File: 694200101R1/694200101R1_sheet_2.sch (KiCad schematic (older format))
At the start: 87 parts, among them U4 M24M02-DRMN6TP, U5 IS31FL3733B-QFLS4-TR, U6 IS31FL3733B-QFLS4-TR

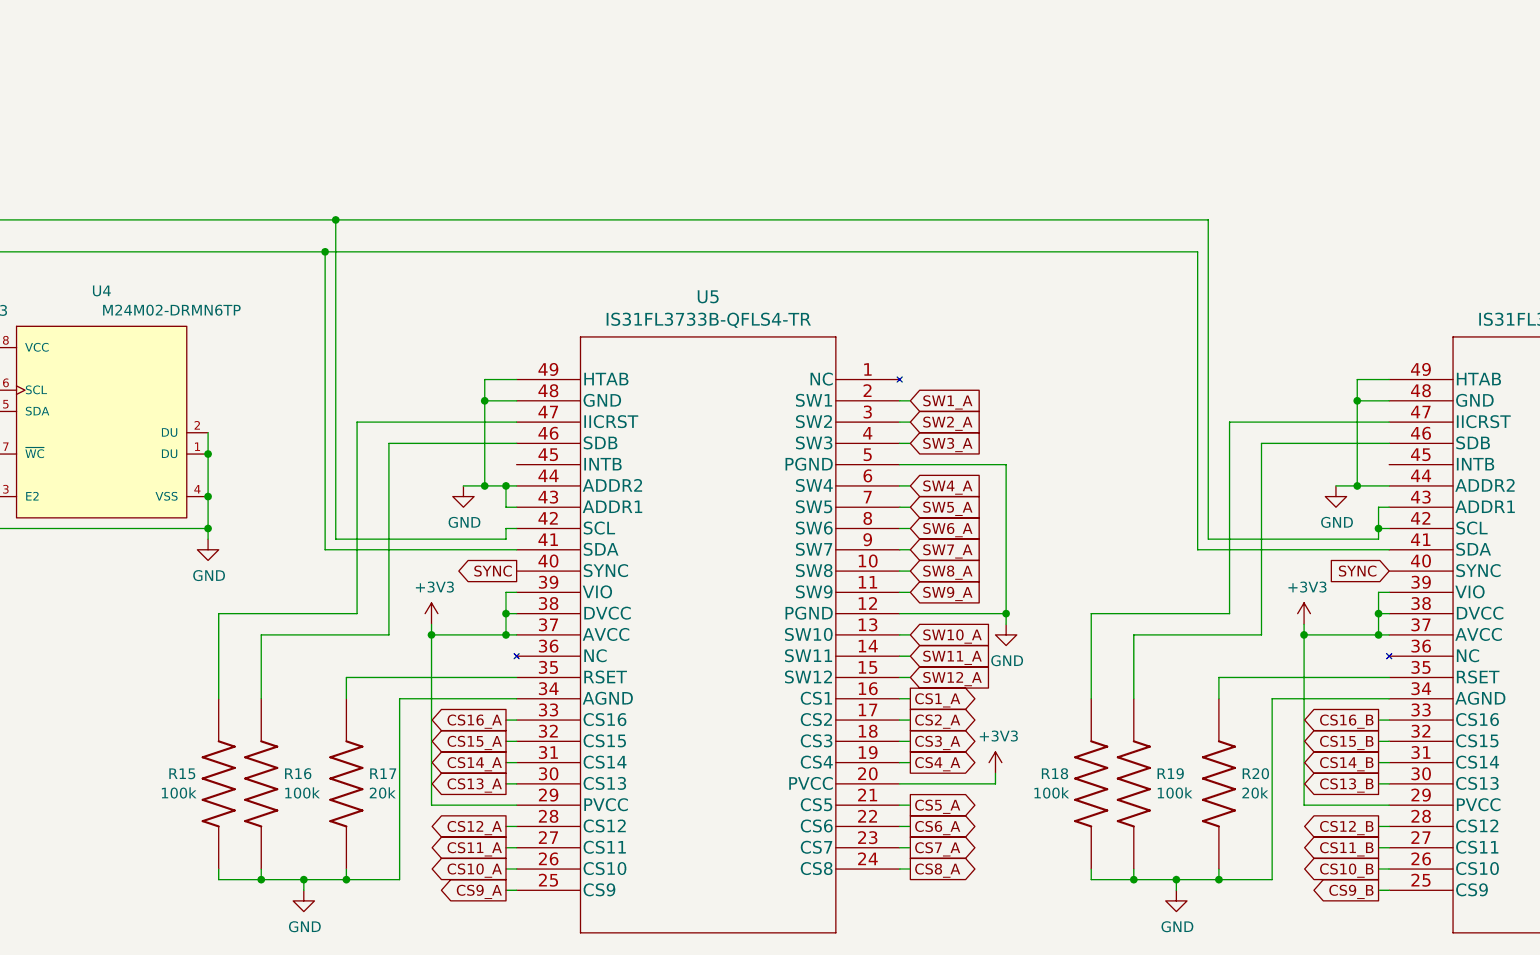
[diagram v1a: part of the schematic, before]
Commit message: Fixed incorrect pull-down resistors
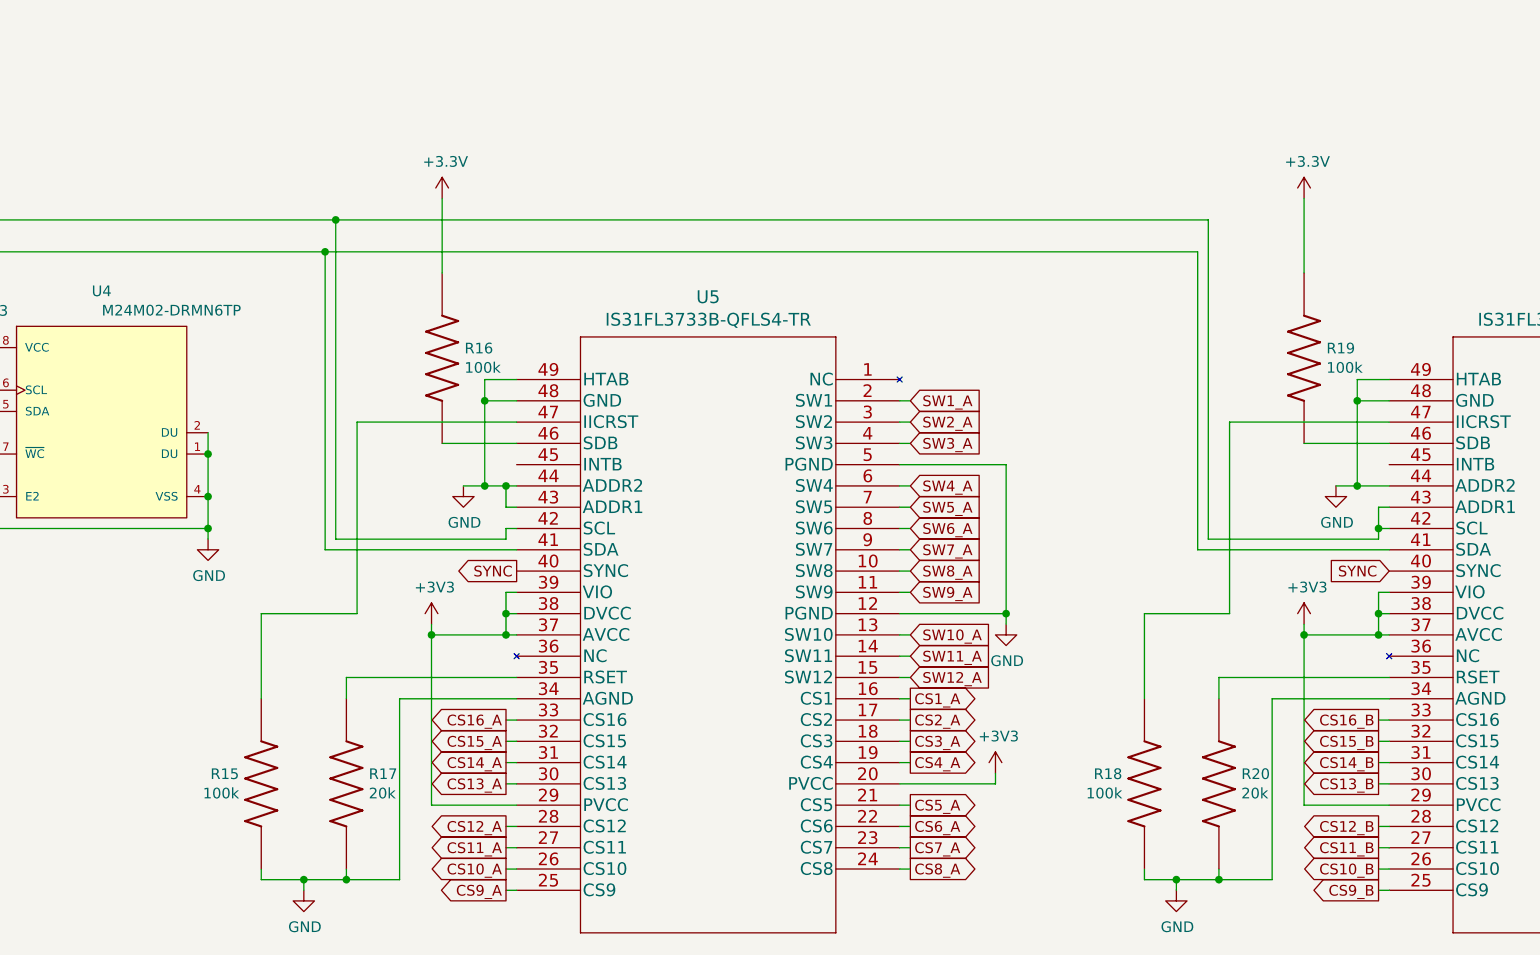
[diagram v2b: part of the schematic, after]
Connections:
- net +3V3: now also R16.1, R19.1
- net GND: no longer R16.2, R19.2
- net at U5.46 (SDB): now also R16.2; no longer R16.1
- net at U6.46 (SDB): now also R19.2; no longer R19.1
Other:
- moved on the sheet: R15, R16, R18, R19
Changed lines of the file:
@@
 LED_DRIVER_A\nPWR_FILTER
 Wire Wire Line
-	4000 8050 3400 8050
-Wire Wire Line
-	3400 8050 3400 8950
-Wire Wire Line
-	3400 8950 2800 8950
-Wire Wire Line
-	2800 8950 2800 9250
+	4000 8050 3650 8050
 Connection ~ 3600 8950
 Wire Wire Line
@@
 	3250 7950 3250 8850
 Wire Wire Line
-	3250 8850 2600 8850
+	3250 8850 2800 8850
 Wire Wire Line
-	2600 8850 2600 9250
+	2800 8850 2800 9250
 Wire Wire Line
-	2600 10050 2600 10100
-Wire Wire Line
-	2800 10100 2800 10050
+	2800 10050 2800 10100
 Wire Wire Line
 	4000 9250 3450 9250
@@
 Wire Wire Line
 	3450 10100 3200 10100
-Connection ~ 2800 10100
-Wire Wire Line
-	2600 10100 2800 10100
 Wire Wire Line
 	3600 8900 3600 8950
@@
 Connection ~ 3000 10100
 Wire Wire Line
-	3000 10100 2800 10100
-Wire Wire Line
 	3950 8950 3600 8950
 Wire Wire Line
@@
 Connection ~ 8050 8850
 Connection ~ 8050 8950
-Wire Wire Line
-	8100 8050 7500 8050
-Wire Wire Line
-	7500 8050 7500 8950
-Wire Wire Line
-	7500 8950 6900 8950
-Wire Wire Line
-	6900 8950 6900 9250
 Connection ~ 7700 8950
 Wire Wire Line
@@
 	7350 7950 7350 8850
 Wire Wire Line
-	7350 8850 6700 8850
-Wire Wire Line
-	6700 8850 6700 9250
+	7350 8850 6950 8850
 Wire Wire Line
-	6700 10050 6700 10100
+	6950 8850 6950 9250
 Wire Wire Line
-	6900 10100 6900 10050
+	6950 10050 6950 10100
 Wire Wire Line
 	8100 9250 7550 9250
@@
 Wire Wire Line
 	7550 10100 7300 10100
-Connection ~ 6900 10100
-Wire Wire Line
-	6700 10100 6900 10100
 Wire Wire Line
 	7700 8900 7700 8950
@@
 Connection ~ 7100 10100
 Wire Wire Line
-	7100 10100 6900 10100
-Wire Wire Line
 	8050 8950 7700 8950
 Wire Wire Line
@@
 L Resistor-Lib:RMCF0603FT100K R16
 U 1 1 63EAB8BE
-P 2800 9650
-F 0 "R16" V 2754 9755 50  0000 L CNN
-F 1 "RMCF0603FT100K" H 2500 9450 50  0001 L BNN
-F 2 "Resistor-Libs:RESC1508X55N" H 2800 9650 50  0001 L BNN
-F 3 "" H 2800 9650 50  0001 L BNN
-F 4 "100k" V 2845 9755 50  0000 L CNN "resistance"
-	1    2800 9650
+P 3650 7650
+F 0 "R16" V 3604 7755 50  0000 L CNN
+F 1 "RMCF0603FT100K" H 3350 7450 50  0001 L BNN
+F 2 "Resistor-Libs:RESC1508X55N" H 3650 7650 50  0001 L BNN
+F 3 "" H 3650 7650 50  0001 L BNN
+F 4 "100k" V 3695 7755 50  0000 L CNN "resistance"
+	1    3650 7650
 	0    1    1    0
 $EndComp
@@
 L Resistor-Lib:RMCF0603FT100K R15
 U 1 1 63EB01BF
-P 2600 9650
-F 0 "R15" V 2554 9546 50  0000 R CNN
-F 1 "RMCF0603FT100K" H 2300 9450 50  0001 L BNN
-F 2 "Resistor-Libs:RESC1508X55N" H 2600 9650 50  0001 L BNN
-F 3 "" H 2600 9650 50  0001 L BNN
-F 4 "100k" V 2645 9546 50  0000 R CNN "resistance"
-	1    2600 9650
+P 2800 9650
+F 0 "R15" V 2754 9546 50  0000 R CNN
+F 1 "RMCF0603FT100K" H 2500 9450 50  0001 L BNN
+F 2 "Resistor-Libs:RESC1508X55N" H 2800 9650 50  0001 L BNN
+F 3 "" H 2800 9650 50  0001 L BNN
+F 4 "100k" V 2845 9546 50  0000 R CNN "resistance"
+	1    2800 9650
 	0    1    1    0
 $EndComp
@@
 L Resistor-Lib:RMCF0603FT100K R19
 U 1 1 6409AB23
-P 6900 9650
-F 0 "R19" V 6854 9755 50  0000 L CNN
-F 1 "RMCF0603FT100K" H 6600 9450 50  0001 L BNN
-F 2 "Resistor-Libs:RESC1508X55N" H 6900 9650 50  0001 L BNN
-F 3 "" H 6900 9650 50  0001 L BNN
-F 4 "100k" V 6945 9755 50  0000 L CNN "resistance"
-	1    6900 9650
+P 7700 7650
+F 0 "R19" V 7654 7755 50  0000 L CNN
+F 1 "RMCF0603FT100K" H 7400 7450 50  0001 L BNN
+F 2 "Resistor-Libs:RESC1508X55N" H 7700 7650 50  0001 L BNN
+F 3 "" H 7700 7650 50  0001 L BNN
+F 4 "100k" V 7745 7755 50  0000 L CNN "resistance"
+	1    7700 7650
 	0    1    1    0
 $EndComp
@@
 L Resistor-Lib:RMCF0603FT100K R18
 U 1 1 6409AB2A
-P 6700 9650
-F 0 "R18" V 6654 9546 50  0000 R CNN
-F 1 "RMCF0603FT100K" H 6400 9450 50  0001 L BNN
-F 2 "Resistor-Libs:RESC1508X55N" H 6700 9650 50  0001 L BNN
-F 3 "" H 6700 9650 50  0001 L BNN
-F 4 "100k" V 6745 9546 50  0000 R CNN "resistance"
-	1    6700 9650
+P 6950 9650
+F 0 "R18" V 6904 9546 50  0000 R CNN
+F 1 "RMCF0603FT100K" H 6650 9450 50  0001 L BNN
+F 2 "Resistor-Libs:RESC1508X55N" H 6950 9650 50  0001 L BNN
+F 3 "" H 6950 9650 50  0001 L BNN
+F 4 "100k" V 6995 9546 50  0000 R CNN "resistance"
+	1    6950 9650
 	0    1    1    0
 $EndComp
@@
 Wire Wire Line
 	14850 6900 15900 6900
+$Comp
+L power:+3.3V #PWR?
+U 1 1 60239060
+P 3650 6900
+F 0 "#PWR?" H 3650 6750 50  0001 C CNN
+F 1 "+3.3V" H 3665 7073 50  0000 C CNN
+F 2 "" H 3650 6900 50  0001 C CNN
+F 3 "" H 3650 6900 50  0001 C CNN
+	1    3650 6900
+	1    0    0    -1
+$EndComp
+$Comp
+L power:+3.3V #PWR?
+U 1 1 6031F66E
+P 7700 6900
+F 0 "#PWR?" H 7700 6750 50  0001 C CNN
+F 1 "+3.3V" H 7715 7073 50  0000 C CNN
+F 2 "" H 7700 6900 50  0001 C CNN
+F 3 "" H 7700 6900 50  0001 C CNN
+	1    7700 6900
+	1    0    0    -1
+$EndComp
+Wire Wire Line
+	2800 10100 3000 10100
+Wire Wire Line
+	3650 7250 3650 6900
+Wire Wire Line
+	6950 10100 7100 10100
+Wire Wire Line
+	8100 8050 7700 8050
+Wire Wire Line
+	7700 7250 7700 6900
 $EndSCHEMATC

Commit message: Updated LED Driver Footprint to have termal vias
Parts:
- U5, U6: footprint Lumissil:IS31FL3733B-QFLS4-TR -> Package_DFN_QFN:QFN-48-1EP_6x6mm_P0.4mm_EP4.2x4.2mm_ThermalVias
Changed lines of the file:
@@
 F 0 "U5" H 6700 8137 60  0000 C CNN
 F 1 "IS31FL3733B-QFLS4-TR" H 6700 8031 60  0000 C CNN
-F 2 "Lumissil:IS31FL3733B-QFLS4-TR" H 6700 7990 60  0001 C CNN
+F 2 "Package_DFN_QFN:QFN-48-1EP_6x6mm_P0.4mm_EP4.2x4.2mm_ThermalVias" H 6700 7990 60  0001 C CNN
 F 3 "" H 5800 7750 60  0000 C CNN
 	1    5800 7750
@@
 F 0 "U6" H 10800 8137 60  0000 C CNN
 F 1 "IS31FL3733B-QFLS4-TR" H 10800 8031 60  0000 C CNN
-F 2 "Lumissil:IS31FL3733B-QFLS4-TR" H 10800 7990 60  0001 C CNN
+F 2 "Package_DFN_QFN:QFN-48-1EP_6x6mm_P0.4mm_EP4.2x4.2mm_ThermalVias" H 10800 7990 60  0001 C CNN
 F 3 "" H 9900 7750 60  0000 C CNN
 	1    9900 7750

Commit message: Picked the actual correct footprint for the LED drivers
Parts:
- U5, U6: footprint Package_DFN_QFN:QFN-48-1EP_6x6mm_P0.4mm_EP4.2x4.2mm_ThermalVias -> Package_DFN_QFN:QFN-48-1EP_6x6mm_P0.4mm_EP4.6x4.6mm_ThermalVias
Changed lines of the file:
@@
 F 0 "U5" H 6700 8137 60  0000 C CNN
 F 1 "IS31FL3733B-QFLS4-TR" H 6700 8031 60  0000 C CNN
-F 2 "Package_DFN_QFN:QFN-48-1EP_6x6mm_P0.4mm_EP4.2x4.2mm_ThermalVias" H 6700 7990 60  0001 C CNN
+F 2 "Package_DFN_QFN:QFN-48-1EP_6x6mm_P0.4mm_EP4.6x4.6mm_ThermalVias" H 6700 7990 60  0001 C CNN
 F 3 "" H 5800 7750 60  0000 C CNN
 	1    5800 7750
@@
 F 0 "U6" H 10800 8137 60  0000 C CNN
 F 1 "IS31FL3733B-QFLS4-TR" H 10800 8031 60  0000 C CNN
-F 2 "Package_DFN_QFN:QFN-48-1EP_6x6mm_P0.4mm_EP4.2x4.2mm_ThermalVias" H 10800 7990 60  0001 C CNN
+F 2 "Package_DFN_QFN:QFN-48-1EP_6x6mm_P0.4mm_EP4.6x4.6mm_ThermalVias" H 10800 7990 60  0001 C CNN
 F 3 "" H 9900 7750 60  0000 C CNN
 	1    9900 7750
@@
 	14850 6900 15900 6900
 $Comp
-L power:+3.3V #PWR?
+L power:+3.3V #PWR0111
 U 1 1 60239060
 P 3650 6900
-F 0 "#PWR?" H 3650 6750 50  0001 C CNN
+F 0 "#PWR0111" H 3650 6750 50  0001 C CNN
 F 1 "+3.3V" H 3665 7073 50  0000 C CNN
 F 2 "" H 3650 6900 50  0001 C CNN
@@
 $EndComp
 $Comp
-L power:+3.3V #PWR?
+L power:+3.3V #PWR0112
 U 1 1 6031F66E
 P 7700 6900
-F 0 "#PWR?" H 7700 6750 50  0001 C CNN
+F 0 "#PWR0112" H 7700 6750 50  0001 C CNN
 F 1 "+3.3V" H 7715 7073 50  0000 C CNN
 F 2 "" H 7700 6900 50  0001 C CNN

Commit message: Updated LED Driver Footprint
Updated LED driver footprint to fix back mask being larger than needed and moved the vias closer
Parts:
- U5, U6: footprint Package_DFN_QFN:QFN-48-1EP_6x6mm_P0.4mm_EP4.6x4.6mm_ThermalVias -> cldg:QFN-48-1EP_6x6mm_P0.4mm_EP4.6x4.6mm_ThermalVias
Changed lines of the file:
@@
 F 0 "U5" H 6700 8137 60  0000 C CNN
 F 1 "IS31FL3733B-QFLS4-TR" H 6700 8031 60  0000 C CNN
-F 2 "Package_DFN_QFN:QFN-48-1EP_6x6mm_P0.4mm_EP4.6x4.6mm_ThermalVias" H 6700 7990 60  0001 C CNN
+F 2 "cldg:QFN-48-1EP_6x6mm_P0.4mm_EP4.6x4.6mm_ThermalVias" H 6700 7990 60  0001 C CNN
 F 3 "" H 5800 7750 60  0000 C CNN
 	1    5800 7750
@@
 F 0 "U6" H 10800 8137 60  0000 C CNN
 F 1 "IS31FL3733B-QFLS4-TR" H 10800 8031 60  0000 C CNN
-F 2 "Package_DFN_QFN:QFN-48-1EP_6x6mm_P0.4mm_EP4.6x4.6mm_ThermalVias" H 10800 7990 60  0001 C CNN
+F 2 "cldg:QFN-48-1EP_6x6mm_P0.4mm_EP4.6x4.6mm_ThermalVias" H 10800 7990 60  0001 C CNN
 F 3 "" H 9900 7750 60  0000 C CNN
 	1    9900 7750

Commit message: Updated LED driver footprint with wider vias
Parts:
- U5, U6: footprint cldg:QFN-48-1EP_6x6mm_P0.4mm_EP4.6x4.6mm_ThermalVias -> cldg:QFN-48_EP_6.6x6.6_Pitch0.4mm
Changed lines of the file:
@@
 F 0 "U5" H 6700 8137 60  0000 C CNN
 F 1 "IS31FL3733B-QFLS4-TR" H 6700 8031 60  0000 C CNN
-F 2 "cldg:QFN-48-1EP_6x6mm_P0.4mm_EP4.6x4.6mm_ThermalVias" H 6700 7990 60  0001 C CNN
+F 2 "cldg:QFN-48_EP_6.6x6.6_Pitch0.4mm" H 6700 7990 60  0001 C CNN
 F 3 "" H 5800 7750 60  0000 C CNN
 	1    5800 7750
@@
 F 0 "U6" H 10800 8137 60  0000 C CNN
 F 1 "IS31FL3733B-QFLS4-TR" H 10800 8031 60  0000 C CNN
-F 2 "cldg:QFN-48-1EP_6x6mm_P0.4mm_EP4.6x4.6mm_ThermalVias" H 10800 7990 60  0001 C CNN
+F 2 "cldg:QFN-48_EP_6.6x6.6_Pitch0.4mm" H 10800 7990 60  0001 C CNN
 F 3 "" H 9900 7750 60  0000 C CNN
 	1    9900 7750
